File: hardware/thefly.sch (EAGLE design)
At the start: 37 parts, among them IC1 AP7313-1.8, J1 54-00298-HOLES, U1 SGTL5000XNLA3, U2 MAX4466EXK

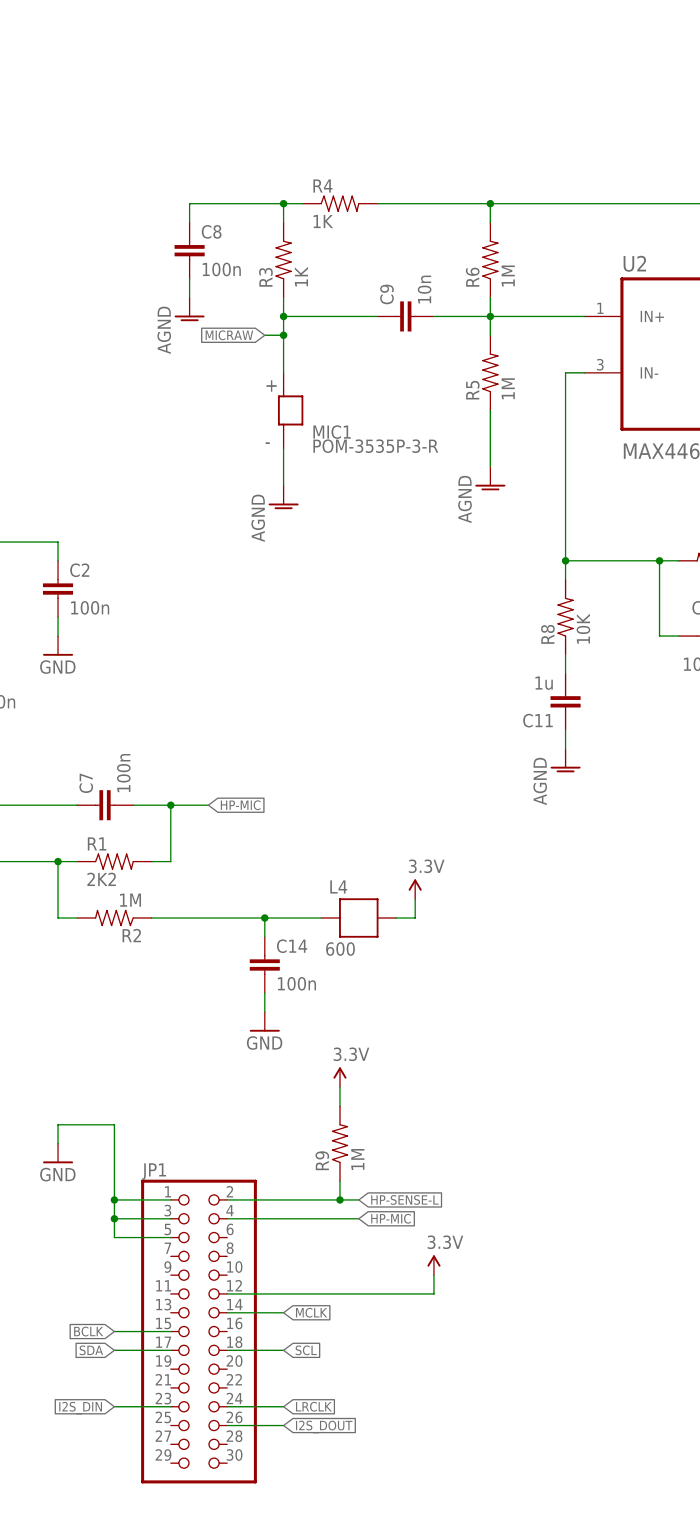
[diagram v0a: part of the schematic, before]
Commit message: pcb layout changes, removed L4, added comments
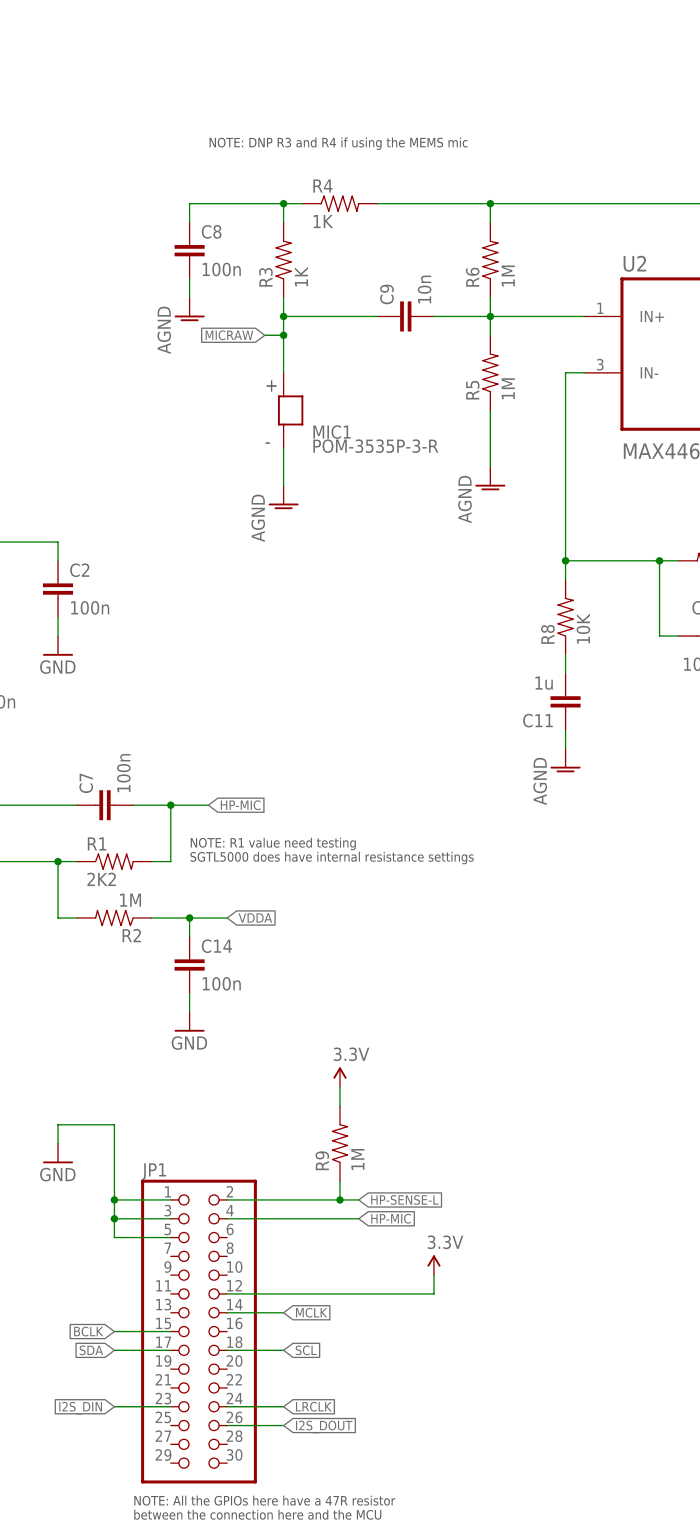
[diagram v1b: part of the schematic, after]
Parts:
- removed L4: 600, thefly:FB
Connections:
- removed net N$1: C14.1, L4.P$2, R2.1
- net 3.3V: no longer L4.P$1
- net VDDA: now also C14.1, R2.1
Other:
- note added: "NOTE: All the GPIOs here have a 47R resistor between the connection here and the MCU"
- note added: "NOTE: DNP R3 and R4 if using the MEMS mic"
- note added: "NOTE: R1 value need testing SGTL5000 does have internal resistance settings"
- moved on the sheet: C14
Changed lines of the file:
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@@
 <part name="C7" library="thefly" deviceset="CAP" device="0603-CAP" value="100n"/>
 <part name="R2" library="thefly" deviceset="RESISTOR" device="0603-RES" value="1M"/>
-<part name="P+3" library="thefly" deviceset="3.3V" device=""/>
 <part name="L2" library="thefly" deviceset="FB" device="" value="600"/>
 <part name="L3" library="thefly" deviceset="FB" device="" value="600"/>
@@
 <part name="C13" library="thefly" deviceset="CAP" device="0603-CAP" value="100n"/>
 <part name="AGND8" library="thefly" deviceset="AGND" device=""/>
-<part name="L4" library="thefly" deviceset="FB" device="" value="600"/>
 <part name="C14" library="thefly" deviceset="CAP" device="0603-CAP" value="100n"/>
 <part name="GND11" library="thefly" deviceset="GND" device=""/>
@@
 <sheet>
 <plain>
+<text x="132.08" y="-83.82" size="1.27" layer="97">NOTE: All the GPIOs here have a 47R resistor
+between the connection here and the MCU</text>
+<text x="142.24" y="101.6" size="1.27" layer="97">NOTE: DNP R3 and R4 if using the MEMS mic</text>
+<text x="139.7" y="5.08" size="1.27" layer="97">NOTE: R1 value need testing
+SGTL5000 does have internal resistance settings</text>
 </plain>
 <instances>
@@
 <instance part="C7" gate="G$1" x="129.54" y="12.7" rot="R90"/>
 <instance part="R2" gate="G$1" x="129.54" y="-2.54" rot="R180"/>
-<instance part="P+3" gate="G$1" x="170.18" y="0"/>
 <instance part="L2" gate="G$1" x="256.54" y="81.28"/>
 <instance part="L3" gate="G$1" x="241.3" y="66.04"/>
@@
 <instance part="C13" gate="G$1" x="236.22" y="25.4"/>
 <instance part="AGND8" gate="VR1" x="228.6" y="27.94"/>
-<instance part="L4" gate="G$1" x="162.56" y="-2.54"/>
-<instance part="C14" gate="G$1" x="149.86" y="-10.16"/>
-<instance part="GND11" gate="1" x="149.86" y="-17.78"/>
+<instance part="C14" gate="G$1" x="139.7" y="-10.16"/>
+<instance part="GND11" gate="1" x="139.7" y="-17.78"/>
 <instance part="U$5" gate="G$1" x="-2.54" y="20.32"/>
 </instances>
@@
 <pinref part="C14" gate="G$1" pin="2"/>
 <pinref part="GND11" gate="1" pin="GND"/>
-<wire x1="149.86" y1="-12.7" x2="149.86" y2="-15.24" width="0.1524" layer="91"/>
+<wire x1="139.7" y1="-12.7" x2="139.7" y2="-15.24" width="0.1524" layer="91"/>
 </segment>
 </net>
@@
 <wire x1="93.98" y1="53.34" x2="91.44" y2="53.34" width="0.1524" layer="91"/>
 <label x="91.44" y="53.34" size="1.27" layer="95" rot="R180" xref="yes"/>
+</segment>
+<segment>
+<pinref part="R2" gate="G$1" pin="1"/>
+<wire x1="144.78" y1="-2.54" x2="139.7" y2="-2.54" width="0.1524" layer="91"/>
+<pinref part="C14" gate="G$1" pin="1"/>
+<wire x1="139.7" y1="-2.54" x2="134.62" y2="-2.54" width="0.1524" layer="91"/>
+<wire x1="139.7" y1="-5.08" x2="139.7" y2="-2.54" width="0.1524" layer="91"/>
+<junction x="139.7" y="-2.54"/>
+<label x="144.78" y="-2.54" size="1.27" layer="95" xref="yes"/>
 </segment>
 </net>
@@
 <pinref part="R9" gate="G$1" pin="2"/>
 <wire x1="160.02" y1="-25.4" x2="160.02" y2="-27.94" width="0.1524" layer="91"/>
-</segment>
-<segment>
-<pinref part="P+3" gate="G$1" pin="3.3V"/>
-<wire x1="170.18" y1="0" x2="170.18" y2="-2.54" width="0.1524" layer="91"/>
-<pinref part="L4" gate="G$1" pin="P$1"/>
-<wire x1="170.18" y1="-2.54" x2="167.64" y2="-2.54" width="0.1524" layer="91"/>
 </segment>
 </net>
@@
 </segment>
 </net>
-<net name="N$1" class="0">
-<segment>
-<pinref part="R2" gate="G$1" pin="1"/>
-<pinref part="L4" gate="G$1" pin="P$2"/>
-<wire x1="157.48" y1="-2.54" x2="149.86" y2="-2.54" width="0.1524" layer="91"/>
-<pinref part="C14" gate="G$1" pin="1"/>
-<wire x1="149.86" y1="-2.54" x2="134.62" y2="-2.54" width="0.1524" layer="91"/>
-<wire x1="149.86" y1="-5.08" x2="149.86" y2="-2.54" width="0.1524" layer="91"/>
-<junction x="149.86" y="-2.54"/>
-</segment>
-</net>
 </nets>
 </sheet>
@@
 </schematic>
 </drawing>
+<compatibility>
+<note version="6.3" minversion="6.2.2" severity="warning">
+Since Version 6.2.2 text objects can contain more than one line,
+which will not be processed correctly with this version.
+</note>
+</compatibility>
 </eagle>

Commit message: pcb layout use ledc pwm mclk
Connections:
- net MCLK: now also JP1.16; no longer JP1.14
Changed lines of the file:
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@@
 </segment>
 <segment>
-<pinref part="JP1" gate="A" pin="14"/>
-<wire x1="144.78" y1="-55.88" x2="152.4" y2="-55.88" width="0.1524" layer="91"/>
-<label x="152.4" y="-55.88" size="1.27" layer="95" xref="yes"/>
+<pinref part="JP1" gate="A" pin="16"/>
+<wire x1="144.78" y1="-58.42" x2="152.4" y2="-58.42" width="0.1524" layer="91"/>
+<label x="152.4" y="-58.42" size="1.27" layer="95" xref="yes"/>
 </segment>
 </net>

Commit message: layout change to add dc block on mic path
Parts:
- added C15: 100n, thefly:CAP0603-CAP
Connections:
- new net ASDASDASD: C10.2, C14.1, R7.1, U2.OUT
- net GND: now also C15.2; no longer C14.2
- net MIC2: now also C14.2; no longer C10.2, R7.1, U2.OUT
- net VDDA: now also C15.1; no longer C14.1
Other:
- moved on the sheet: C14
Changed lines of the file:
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@@
 <part name="C13" library="thefly" deviceset="CAP" device="0603-CAP" value="100n"/>
 <part name="AGND8" library="thefly" deviceset="AGND" device=""/>
-<part name="C14" library="thefly" deviceset="CAP" device="0603-CAP" value="100n"/>
+<part name="C15" library="thefly" deviceset="CAP" device="0603-CAP" value="100n"/>
 <part name="GND11" library="thefly" deviceset="GND" device=""/>
 <part name="U$5" library="thefly" deviceset="THE-FLY-LOGO" device=""/>
+<part name="C14" library="thefly" deviceset="CAP" device="0603-CAP" value="100n"/>
 </parts>
 <sheets>
@@
 <instance part="C13" gate="G$1" x="236.22" y="25.4"/>
 <instance part="AGND8" gate="VR1" x="228.6" y="27.94"/>
-<instance part="C14" gate="G$1" x="139.7" y="-10.16"/>
+<instance part="C15" gate="G$1" x="139.7" y="-10.16"/>
 <instance part="GND11" gate="1" x="139.7" y="-17.78"/>
 <instance part="U$5" gate="G$1" x="-2.54" y="20.32"/>
+<instance part="C14" gate="G$1" x="279.4" y="73.66" rot="R90"/>
 </instances>
 <busses>
@@
 </segment>
 <segment>
-<pinref part="C14" gate="G$1" pin="2"/>
+<pinref part="C15" gate="G$1" pin="2"/>
 <pinref part="GND11" gate="1" pin="GND"/>
 <wire x1="139.7" y1="-12.7" x2="139.7" y2="-15.24" width="0.1524" layer="91"/>
@@
 <pinref part="R2" gate="G$1" pin="1"/>
 <wire x1="144.78" y1="-2.54" x2="139.7" y2="-2.54" width="0.1524" layer="91"/>
-<pinref part="C14" gate="G$1" pin="1"/>
+<pinref part="C15" gate="G$1" pin="1"/>
 <wire x1="139.7" y1="-2.54" x2="134.62" y2="-2.54" width="0.1524" layer="91"/>
 <wire x1="139.7" y1="-5.08" x2="139.7" y2="-2.54" width="0.1524" layer="91"/>
@@
 <net name="MIC2" class="0">
 <segment>
-<pinref part="U2" gate="A" pin="OUT"/>
-<wire x1="228.6" y1="73.66" x2="256.54" y2="73.66" width="0.1524" layer="91"/>
-<label x="264.16" y="73.66" size="1.27" layer="95" xref="yes"/>
-<pinref part="R7" gate="G$1" pin="1"/>
-<wire x1="256.54" y1="73.66" x2="264.16" y2="73.66" width="0.1524" layer="91"/>
-<wire x1="215.9" y1="45.72" x2="218.44" y2="45.72" width="0.1524" layer="91"/>
-<wire x1="218.44" y1="45.72" x2="256.54" y2="45.72" width="0.1524" layer="91"/>
-<wire x1="256.54" y1="45.72" x2="256.54" y2="73.66" width="0.1524" layer="91"/>
-<pinref part="C10" gate="G$1" pin="2"/>
-<wire x1="213.36" y1="35.56" x2="218.44" y2="35.56" width="0.1524" layer="91"/>
-<wire x1="218.44" y1="35.56" x2="218.44" y2="45.72" width="0.1524" layer="91"/>
-<junction x="256.54" y="73.66"/>
-<junction x="218.44" y="45.72"/>
-</segment>
-<segment>
 <pinref part="U1" gate="G$1" pin="LINEIN_R"/>
-<wire x1="48.26" y1="40.64" x2="45.72" y2="40.64" width="0.1524" layer="91"/>
-<label x="45.72" y="40.64" size="1.27" layer="95" rot="R180" xref="yes"/>
+<label x="20.32" y="40.64" size="1.27" layer="95" rot="R180" xref="yes"/>
+<wire x1="48.26" y1="40.64" x2="20.32" y2="40.64" width="0.1524" layer="91"/>
+</segment>
+<segment>
+<wire x1="281.94" y1="73.66" x2="284.48" y2="73.66" width="0.1524" layer="91"/>
+<pinref part="C14" gate="G$1" pin="2"/>
+<label x="284.48" y="73.66" size="1.27" layer="95" xref="yes"/>
 </segment>
 </net>
@@
 </segment>
 </net>
+<net name="ASDASDASD" class="0">
+<segment>
+<pinref part="U2" gate="A" pin="OUT"/>
+<wire x1="228.6" y1="73.66" x2="256.54" y2="73.66" width="0.1524" layer="91"/>
+<pinref part="R7" gate="G$1" pin="1"/>
+<wire x1="256.54" y1="73.66" x2="274.32" y2="73.66" width="0.1524" layer="91"/>
+<wire x1="215.9" y1="45.72" x2="218.44" y2="45.72" width="0.1524" layer="91"/>
+<wire x1="218.44" y1="45.72" x2="256.54" y2="45.72" width="0.1524" layer="91"/>
+<wire x1="256.54" y1="45.72" x2="256.54" y2="73.66" width="0.1524" layer="91"/>
+<pinref part="C10" gate="G$1" pin="2"/>
+<wire x1="213.36" y1="35.56" x2="218.44" y2="35.56" width="0.1524" layer="91"/>
+<wire x1="218.44" y1="35.56" x2="218.44" y2="45.72" width="0.1524" layer="91"/>
+<junction x="256.54" y="73.66"/>
+<junction x="218.44" y="45.72"/>
+<pinref part="C14" gate="G$1" pin="1"/>
+</segment>
+</net>

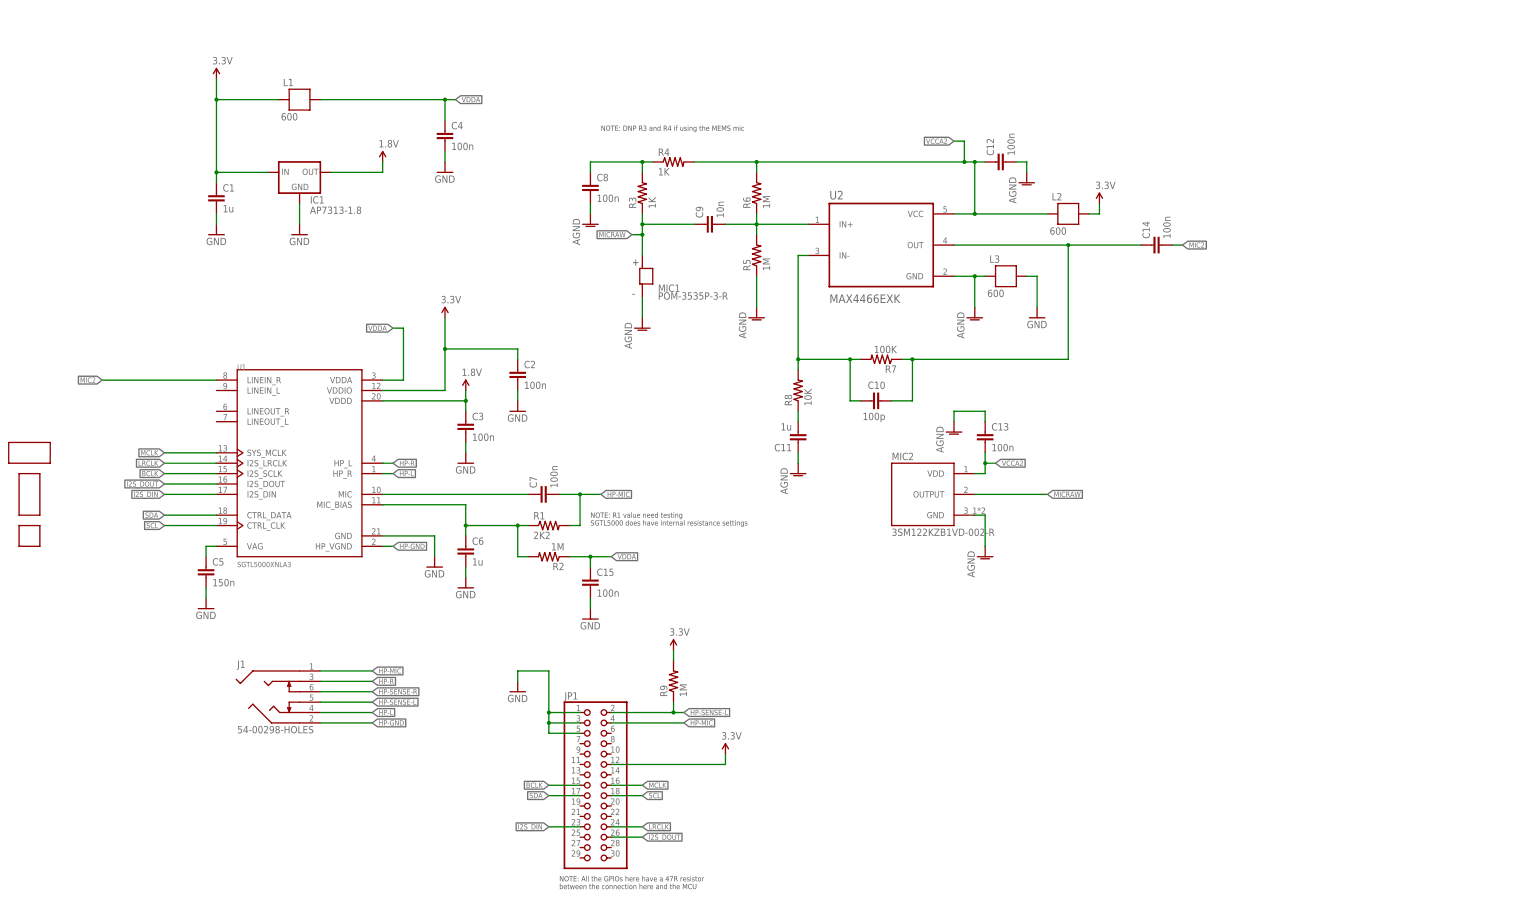
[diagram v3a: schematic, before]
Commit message: pcb layout removed agnd, more caps
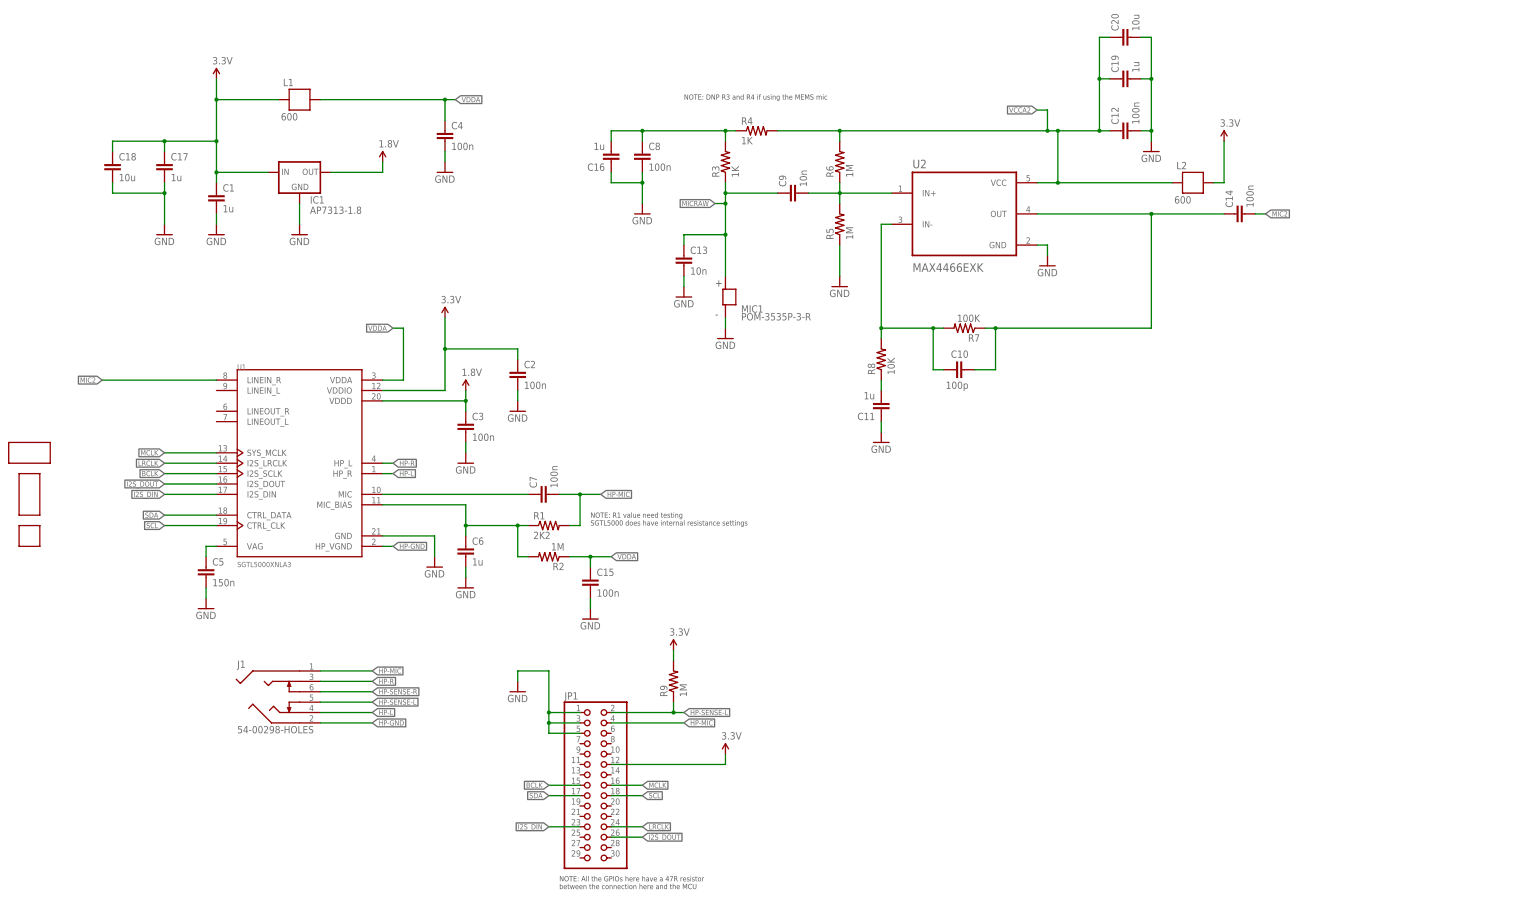
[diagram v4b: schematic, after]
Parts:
- removed L3: 600, thefly:FB
- removed MIC2: 3SM122KZB1VD-002-R, thefly:3SM122KZB1VD-002-R
- added C16, C17, C19: 1u, thefly:CAP0603-CAP
- added C18, C20: 10u, thefly:CAP0603-CAP
- C13: value 100n -> 10n
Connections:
- removed net AGND: C11.1, C12.2, C13.1, C8.2, L3.P$2, MIC1.-, MIC2.GND, R5.1, U2.GND
- net 3.3V: now also C17.1, C18.1
- net GND: now also C11.1, C12.2, C13.2, C16.1, C17.2, C18.2, C19.2, C20.2, C8.2, MIC1.-, R5.1, U2.GND; no longer L3.P$1
- net MICRAW: now also C13.1; no longer MIC2.OUTPUT
- net N$11: now also C16.2
- net VCCA2: now also C19.1, C20.1; no longer C13.2, MIC2.VDD
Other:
- moved on the sheet: C10, C11, C12, C13, C14, C8, C9, L2, MIC1, R3, R4, R5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

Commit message: pcb layout change
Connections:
- net MIC2: now also U1.LINEIN_L
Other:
- note added: "NOTE: testing has shown that the DC blocking diode here is not really needed"
- note added: "NOTE: the mic itself might include a built-in capacitor"
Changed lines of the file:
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@@
 <text x="139.7" y="5.08" size="1.27" layer="97">NOTE: R1 value need testing
 SGTL5000 does have internal resistance settings</text>
+<text x="287.02" y="73.66" size="1.27" layer="97">NOTE: testing has shown that the DC blocking diode here is not really needed</text>
+<text x="160.02" y="66.04" size="1.27" layer="97" align="bottom-right">NOTE: the mic itself might
+include a built-in capacitor</text>
 </plain>
 <instances>
@@
 <pinref part="U1" gate="G$1" pin="LINEIN_R"/>
 <label x="20.32" y="40.64" size="1.27" layer="95" rot="R180" xref="yes"/>
-<wire x1="48.26" y1="40.64" x2="20.32" y2="40.64" width="0.1524" layer="91"/>
-</segment>
-<segment>
+<wire x1="48.26" y1="40.64" x2="45.72" y2="40.64" width="0.1524" layer="91"/>
+<pinref part="U1" gate="G$1" pin="LINEIN_L"/>
+<wire x1="45.72" y1="40.64" x2="20.32" y2="40.64" width="0.1524" layer="91"/>
+<wire x1="48.26" y1="38.1" x2="45.72" y2="38.1" width="0.1524" layer="91"/>
+<wire x1="45.72" y1="38.1" x2="45.72" y2="40.64" width="0.1524" layer="91"/>
+<junction x="45.72" y="40.64"/>
+</segment>
+<segment>
